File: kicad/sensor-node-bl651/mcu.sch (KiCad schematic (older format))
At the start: 13 parts, among them U1 DMP2008UFG-7, Y1 32.768 kHz

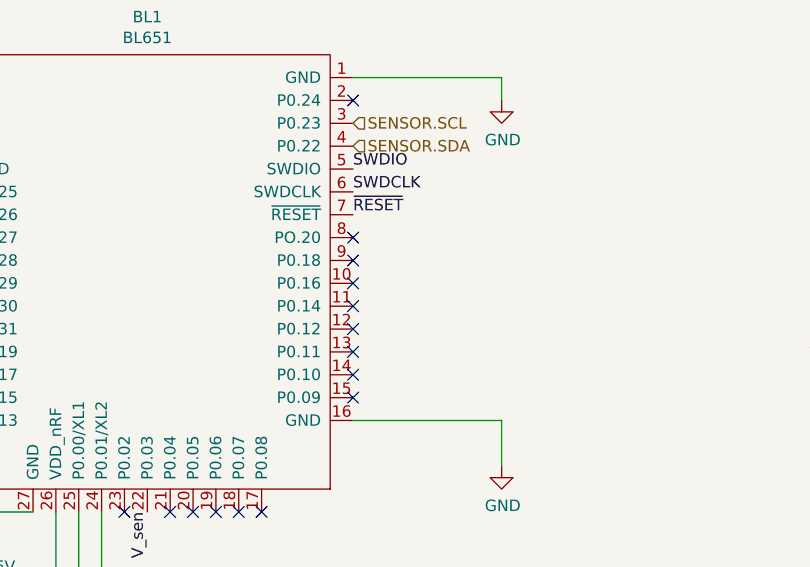
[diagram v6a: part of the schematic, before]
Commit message: add more sensors
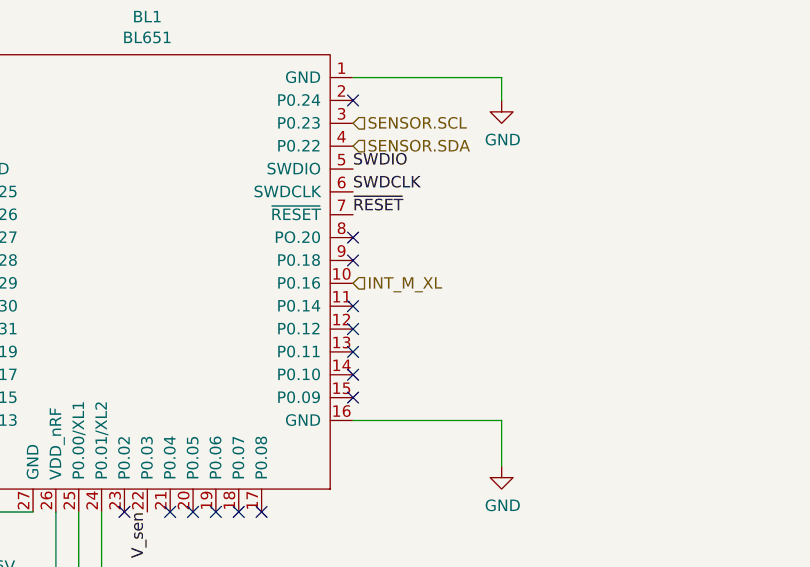
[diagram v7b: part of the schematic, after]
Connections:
- net INT_M_XL: now reaches BL1.10 (P0.16)
- no-connect marks 18 -> 17
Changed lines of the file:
@@
 	8400 5700 9300 5700
 Connection ~ 8300 6250
-NoConn ~ 6600 3050
 NoConn ~ 6600 2250
 NoConn ~ 6600 2850
@@
 	1    0    0    -1
 $EndComp
+Text HLabel 6600 3050 2    50   Input ~ 0
+INT_M_XL
 $EndSCHEMATC

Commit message: add fuses
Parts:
- added F2: Fuse, Fuse:Fuse_0603_1608Metric, symbol Device:Fuse
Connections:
- net GND: now also F2.2; no longer S2.1 (GND)
- net ~SNOOZE: no longer names the net of BL1.31 (P0.19)
- new net: F2.1, S2.1 (GND)
- no-connect marks 17 -> 18
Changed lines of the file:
@@
 	1    0    0    -1
 $EndComp
-Wire Wire Line
-	8900 5900 9300 5900
 Text Label 10500 5800 0    50   ~ 0
 SWDCLK
@@
 	7350 6250 8300 6250
 Wire Wire Line
-	8900 5900 8900 6250
-Wire Wire Line
 	8400 5700 8400 5800
 Wire Wire Line
@@
 Wire Wire Line
 	8400 5700 9300 5700
-Connection ~ 8300 6250
 NoConn ~ 6600 2250
 NoConn ~ 6600 2850
 NoConn ~ 6600 2950
-Text HLabel 4800 3350 0    50   Input ~ 0
-~SNOOZE
 NoConn ~ 4800 3650
-Wire Wire Line
-	8300 6250 8900 6250
 NoConn ~ 5600 4050
 Wire Wire Line
@@
 Text HLabel 6600 3050 2    50   Input ~ 0
 INT_M_XL
+NoConn ~ 4800 3350
+$Comp
+L Device:Fuse F2
+U 1 1 613D5DB1
+P 8800 6250
+F 0 "F2" V 8603 6250 50  0000 C CNN
+F 1 "Fuse" V 8694 6250 50  0000 C CNN
+F 2 "Fuse:Fuse_0603_1608Metric" V 8730 6250 50  0001 C CNN
+F 3 "https://datasheets.avx.com/AccuGuardLC_0402.pdf" H 8800 6250 50  0001 C CNN
+F 4 "478-6871-1-ND" V 8800 6250 50  0001 C CNN "Digi-Key Part Number"
+F 5 "AVX Corporation" V 8800 6250 50  0001 C CNN "Manufacturer"
+F 6 "F0603G0R05FNTR" V 8800 6250 50  0001 C CNN "Manufacturer Part Number"
+F 7 "FUSE BOARD MOUNT 50MA 32VDC 0603" V 8800 6250 50  0001 C CNN "Description"
+	1    8800 6250
+	0    1    1    0
+$EndComp
+Wire Wire Line
+	8950 6250 9150 6250
+Wire Wire Line
+	9150 6250 9150 5900
+Wire Wire Line
+	9150 5900 9300 5900
+Wire Wire Line
+	8650 6250 8300 6250
+Connection ~ 8300 6250
 $EndSCHEMATC
